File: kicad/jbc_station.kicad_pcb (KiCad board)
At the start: 2 copper layers, 125 x 125 mm, 288 parts, among them J1 PWR, J15 Conn_01x07, J2 Conn_01x02, J21 Conn_01x07, J3 Barcode, J4 Front panel, J5 Conn_01x03, J6 Conn_01x05, J7 Conn_01x04, J8 Conn_01x03, J9 Conn_01x07, Q1 BSS138, Q2 BSS138, Q3 BSS138, Q4 AON6448, Q5 AON6448, Q6 AON6448, Q7 AON6448, Q8 AON6448, Q9 AON6448, U1 L78L05_SOT89, U10 STM32F401CCUx, U11 CH9141K, U12 LM5106MM, U13 AD8221ARMZ, U14 LM5106MM, U15 AD8221ARMZ, U16 LM5106MM, U17 AD8221ARMZ, U2 LP2985-3.3, U3 ICL7660, U4 HT7463, U5 HT7463, U6 XC6206PxxxMR, U7 M24C64, U8 INA3221, U9 XC6206PxxxMR, Y1 Crystal, Y2 Crystal

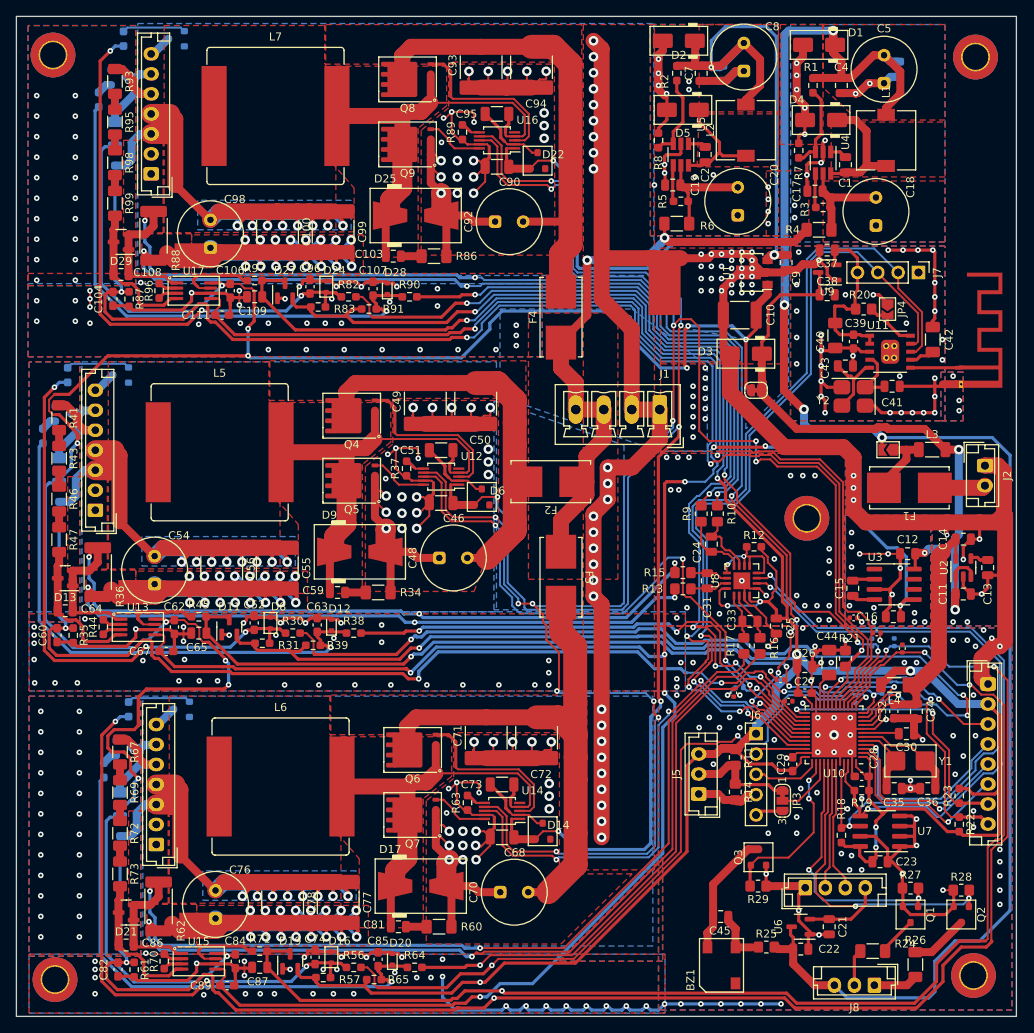
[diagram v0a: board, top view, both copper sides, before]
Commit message: Silkscreen cleanup
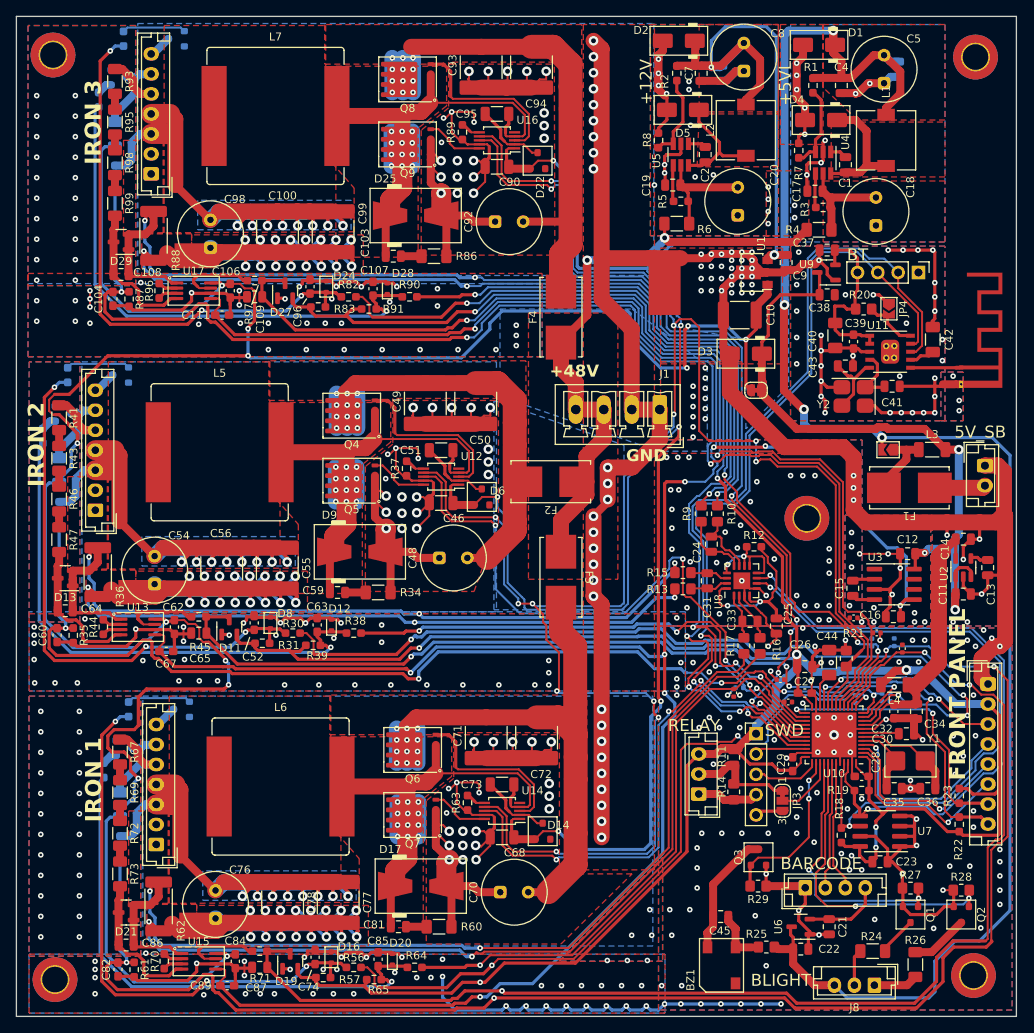
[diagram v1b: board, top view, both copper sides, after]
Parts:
- moved R14 0.20 mm to (89.7, 96.9)
- moved R11 0.20 mm to (89.7, 92.6)
- moved JP4 0.18 mm to (109.1, 36.5)
- moved C61 0.11 mm to (96.5, 85.7)
- moved U9 0.10 mm to (101.2, 32.0)
- moved R21 0.10 mm to (103.7, 80.3)
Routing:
- net Net-(D25-K): track 54.6 -> 67.5 mm, vias 0 -> 12
- net Net-(D17-K): track 54.6 -> 67.5 mm, vias 0 -> 12
- net Net-(Q6-D): track 65.8 -> 78.7 mm, vias 0 -> 12
- net Net-(Q4-D): track 48.5 -> 61.4 mm, vias 0 -> 12
- net Net-(D9-K): track 54.6 -> 67.5 mm, vias 0 -> 12
- net Net-(Q8-D): track 59.9 -> 68.2 mm, vias 0 -> 12
- net GND: track 520.4 -> 517.2 mm, vias 361 -> 404
- net +12V: track 284.2 -> 283.6 mm
- net +3.3V: track 414.1 -> 414.6 mm
- net /PWM_{EN}: track 258.8 -> 258.7 mm, vias 13 -> 12
- net GNDPWR: vias 165 -> 166
- added copper zone on F.Cu, net Net-(D17-K)
- added copper zone on F.Cu, net Net-(D25-K)
- added copper zone on F.Cu, net Net-(D4-K)
- added copper zone on F.Cu, net Net-(D9-K)
- removed copper zone on F.Cu, net Net-(D10-K)
- removed copper zone on F.Cu, net Net-(D18-K)
- removed copper zone on F.Cu, net Net-(D26-K)
- removed copper zone on F.Cu, net Net-(D6-K)
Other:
- board text added: "+12V"
- board text added: "+48V"
- board text added: "+5VL"
- board text added: "5V_SB"
- board text added: "BARCODE"
- board text added: "BLIGHT"
- board text added: "BT"
- board text added: "FRONT PANEL"
- board text added: "GND"
- board text added: "IRON 1"
- board text added: "IRON 2"
- board text added: "IRON 3"
- board text added: "RELAY"
- board text added: "SWD"

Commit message: Various small fixes
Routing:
- net /int-out2/I_{SEN+}: track 109.5 -> 110.8 mm
- net /int-out3/I_{SEN+}: track 109.0 -> 107.8 mm
- net /int-out1/I_{SEN+}: track 83.7 -> 82.4 mm
- net GND: vias 404 -> 410
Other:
- outline, holes or cut-outs redrawn

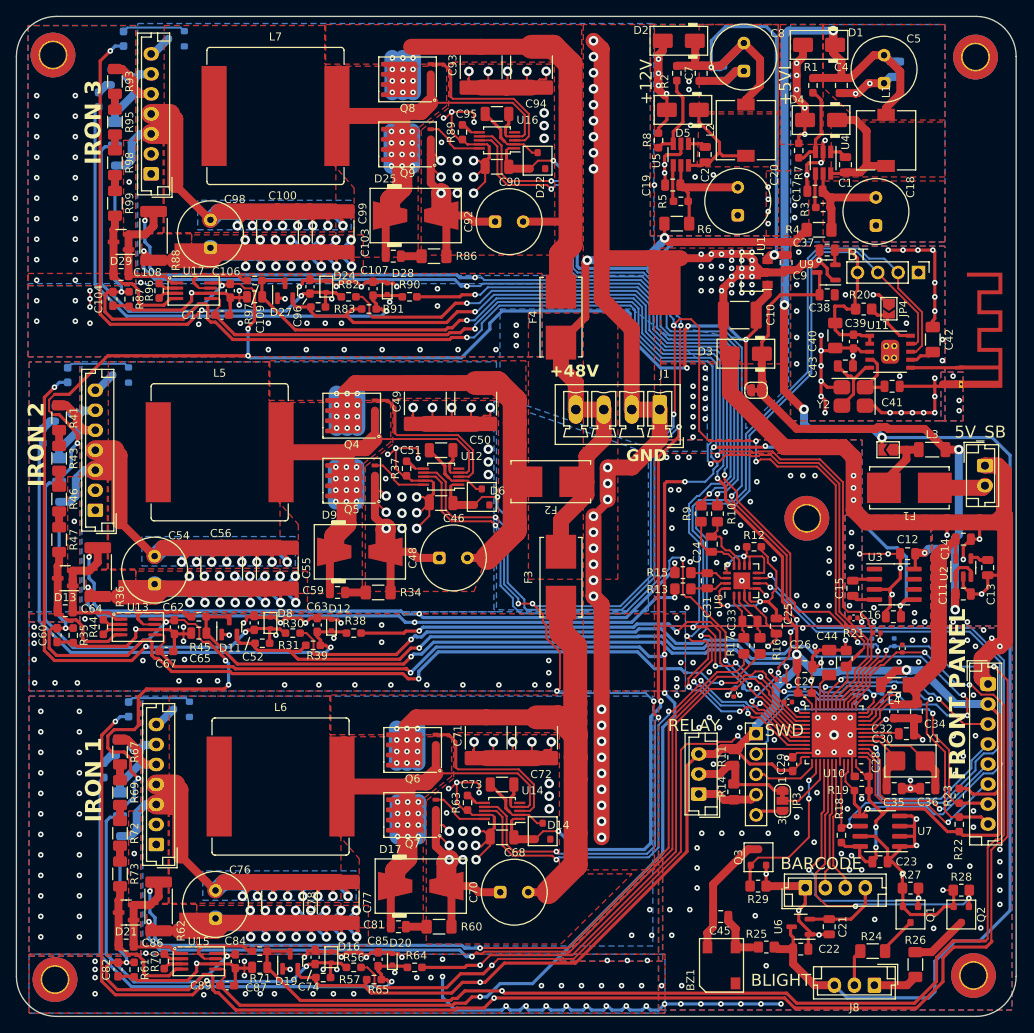
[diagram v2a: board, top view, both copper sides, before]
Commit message: Add logo and text
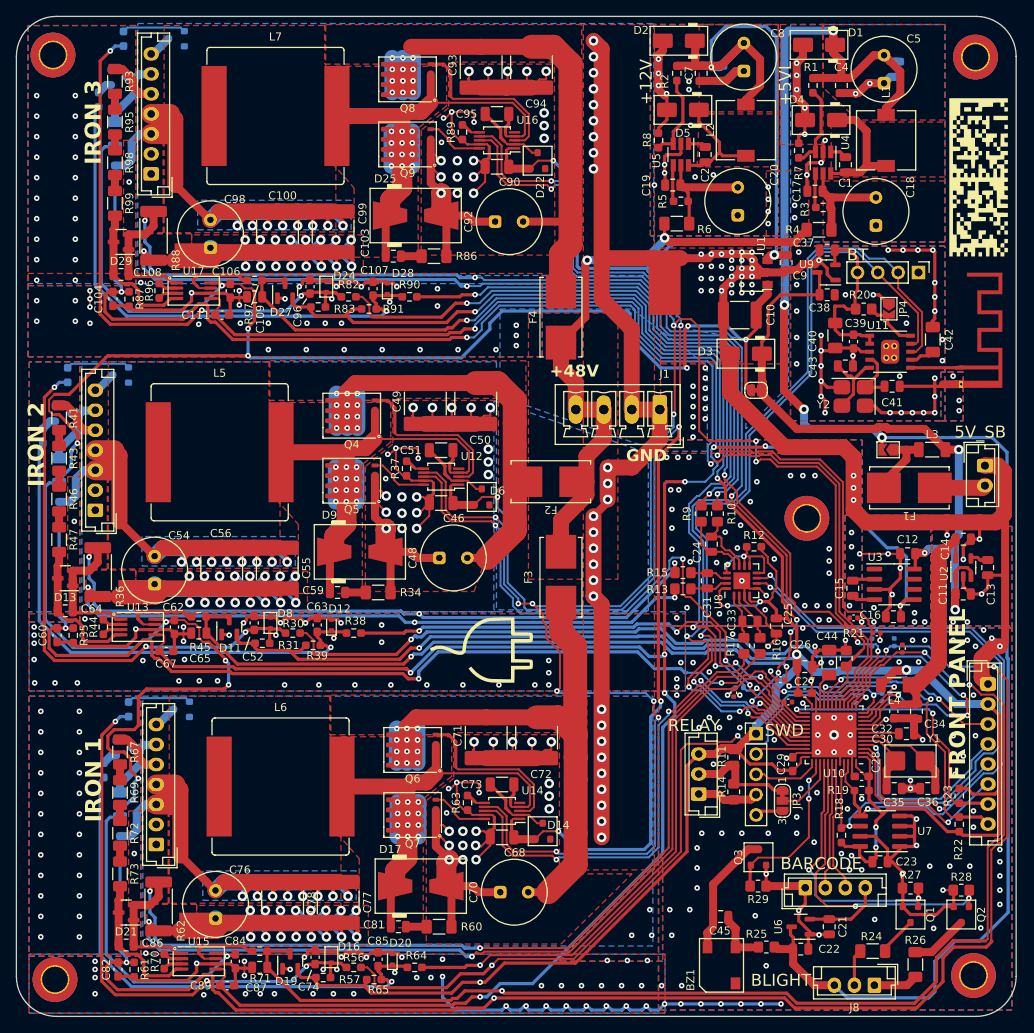
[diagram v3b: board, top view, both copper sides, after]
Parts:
- added G***: LOGO, LOGO, F.Cu at (120.3, 20.2)
- added G***: LOGO, LOGO, F.Cu at (58.2, 79.2)
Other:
- board text added: "3x CHANNEL SOLDERING IRON CONTROLLER"
